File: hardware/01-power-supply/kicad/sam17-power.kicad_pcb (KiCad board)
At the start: 2 copper layers, 100 x 150 mm, 37 parts, among them J1 TerminalBlock_MaiXu_MX126-5.0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, J2 Molex_KK-254_AE-6410-04A_1x04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, J3 TerminalBlock_MaiXu_MX126-5.0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, J4 TerminalBlock_MaiXu_MX126-5.0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, J5 Faston_6.3x0.8mm_PCB_2Leg_P5.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, J6 Molex_KK-254_AE-6410-02A_1x02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, U1 TO-220-3_Vertical, U2 TO-220-3_Vertical, U3 TO-220-3_Vertical

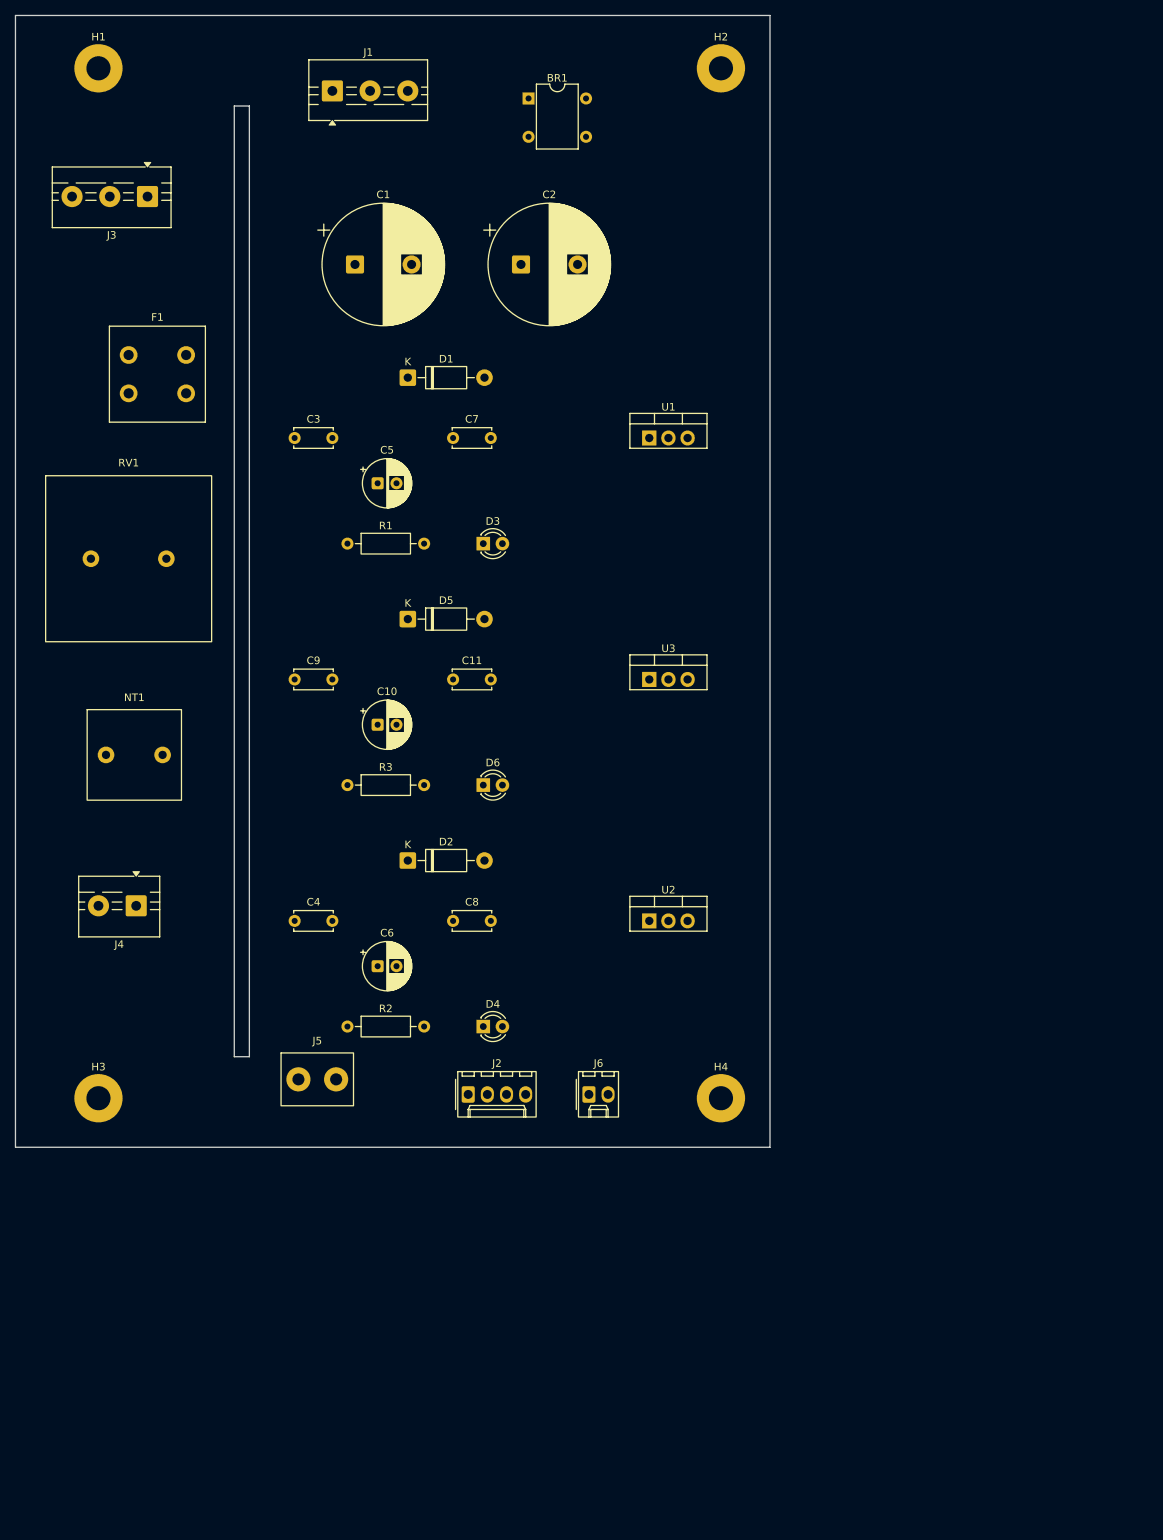
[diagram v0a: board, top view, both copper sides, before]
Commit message: Route module 1 PCB as a verified star ground, no copper pour
Fase 3: la placa queda ruteada entera. DRC de KiCad 0 infracciones y 0 pads
sin conectar. Dos capas, F para carriles y lado de red, B para el arbol de
masa y los bajantes, una sola via en toda la placa.

NO HAY PLANO DE MASA y es a proposito. Un pour une todo con todo por el camino
mas corto, o sea lo contrario de la estrella de sec.7 y del retorno dedicado
de sec.10.1. GND es un arbol que sale de C1.2 (el bulk del riel positivo) y
cada rama muere en su grupo funcional. El retorno del +5V (J6.2) sube por el
canto derecho, la unica columna sin ramas, y entra a la estrella por su propia
via sin tocar ninguna otra.

Que la masa sea un arbol NO SE VE mirando el dibujo — un bucle se ve igual que
una rama — asi que build_pcb.py lo comprueba con union-find sobre los extremos
de los tramos y aborta si encuentra uno. Da 0.

Tampoco se uso autorouter, y no solo por falta del jar: un autorouter respeta
la conectividad y se pasa la topologia por el forro, que aqui es justo lo que
importa.

Lo que fue apareciendo, cada uno con su vuelta:

- Mi verificador comparaba pista contra pista y NO pista contra pad. Con eso
  el trazado salia "limpio" mientras el DRC encontraba cinco cortocircuitos:
  la espina de masa cruzando D5.1 y D2.1, el bajante de -12V rozando el anodo
  de D4, y un LED sin girar. Un pad es cobre igual que una pista; no mirarlo
  era mirar media placa. Ahora se comprueba y da 0.
- Los tres reguladores sacan la salida por el mismo x=89.1, asi que un bajante
  vertical corta a los otros dos. Tres columnas (90/93/97) y el que acaba mas
  a la izquierda gira mas arriba.
- Los tres LED tenian el anodo al lado contrario de su resistencia: la pista
  tenia que atravesar el pad del catodo. Girados 180.
- La espina de masa iba por x=52.5 y D5.1/D2.1 estan en x=52. Movida a x=56,
  por el pasillo de 2.1 mm entre los pads de las resistencias y los ceramicos.
- RED_230V baja de 2.5 a 2.0 mm de separacion. No es relaj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
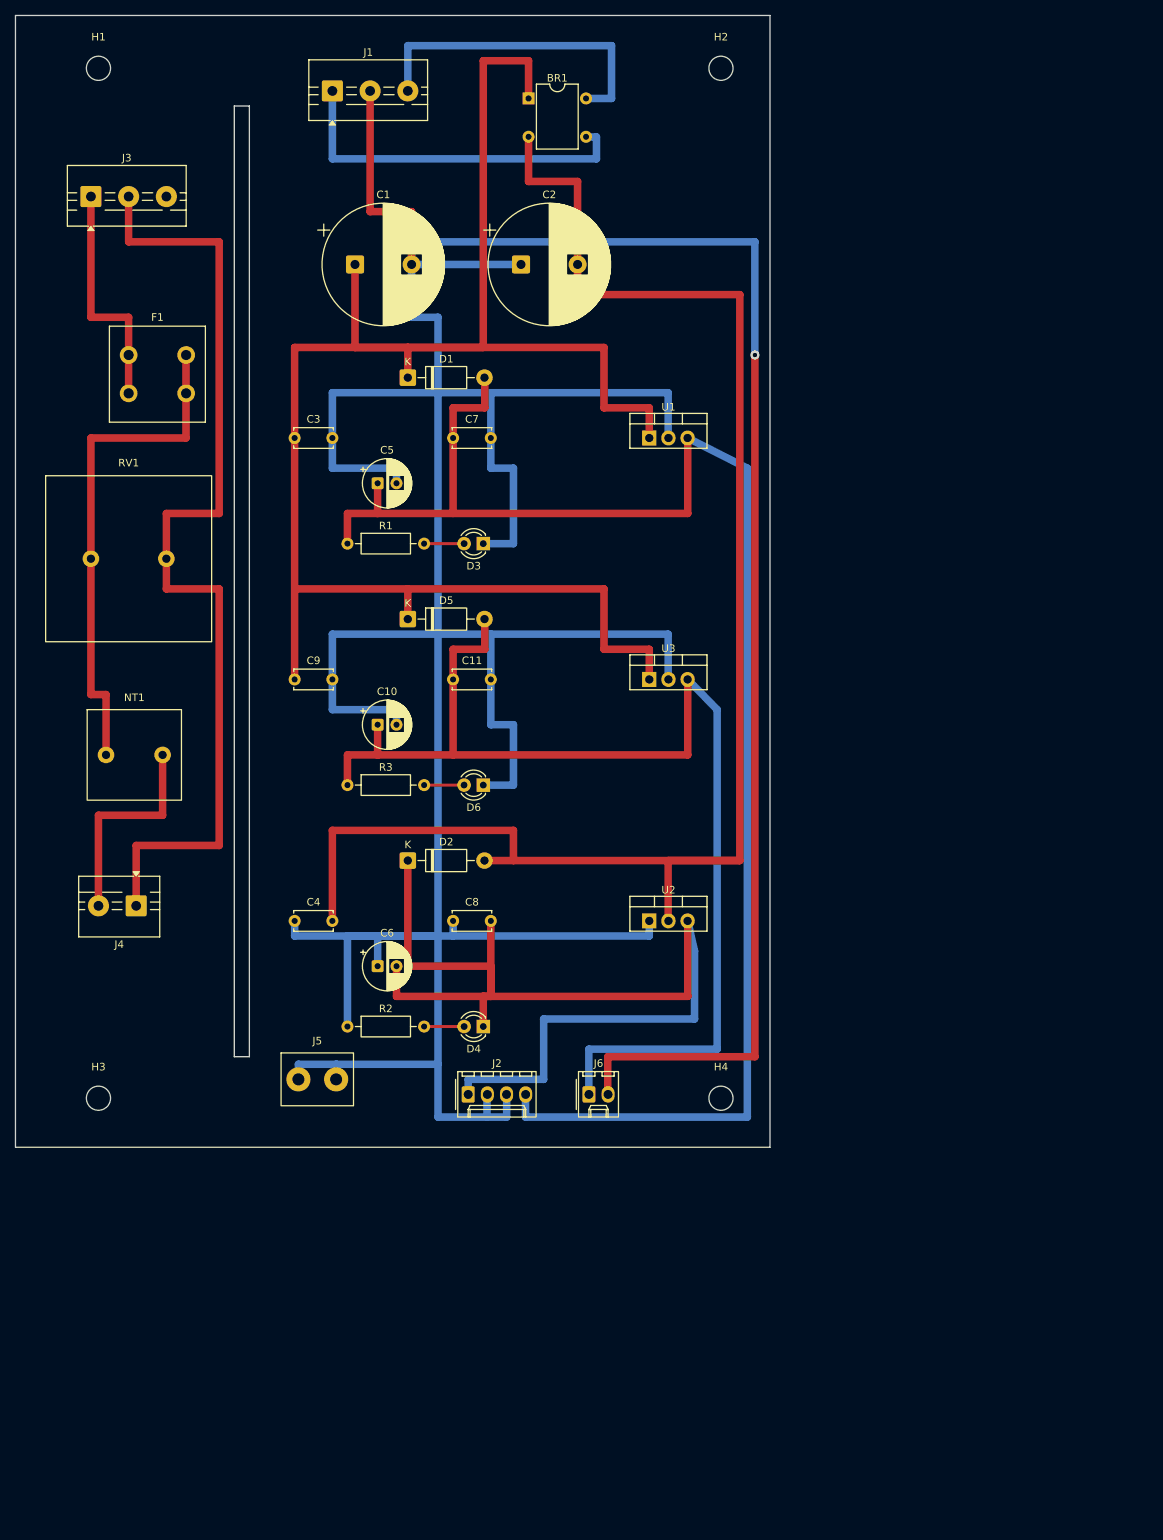
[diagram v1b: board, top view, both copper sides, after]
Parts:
- H1, H2, H3, H4: value MountingHole_3.2mm_M3_Pad -> MountingHole_3.2mm_M3; footprint MountingHole_3.2mm_M3_Pad -> MountingHole_3.2mm_M3
- moved J3 7.50 mm to (10.0, 24.0), turned to 0 degrees
- turned D3 to 180 degrees
- turned D4 to 180 degrees
- turned D6 to 180 degrees
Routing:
- net GND: track 0.00 -> 663.1 mm, vias 0 -> 1
- net /VRAW+: track 0.00 -> 247.0 mm
- net /VRAW-: track 0.00 -> 215.2 mm
- net +12V: track 0.00 -> 212.6 mm
- net +5V: track 0.00 -> 158.9 mm
- net -12V: track 0.00 -> 149.7 mm
- net /N: track 0.00 -> 131.0 mm
- net /L_F: track 0.00 -> 67.6 mm
- net /SEC_A: track 0.00 -> 48.3 mm
- net /SEC_B: track 0.00 -> 43.4 mm
- net /L: track 0.00 -> 31.1 mm
- net /L_TR: track 0.00 -> 28.5 mm
- net Net-(D6-A): track 0.00 -> 5.30 mm
- net Net-(D4-A): track 0.00 -> 5.30 mm
- net Net-(D3-A): track 0.00 -> 5.30 mm

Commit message: Re-lay out module 1 PCB for the LDO respin: 150x200, rail columns
La placa pasa de 100x150 a 150x200. No es capricho: los disipadores pasan de
25x25 a 42x38 (Fischer SK 129/38,1) y tres en fila piden 136 mm de ancho.

DOS DECISIONES DE MAQUETA:

1) La franja de red pasa de columna VERTICAL a la izquierda a fila HORIZONTAL
   arriba, y la barrera con ella. Con la franja vertical harian falta 175 mm de
   ancho (27 de franja + 6 de barrera + 136 de disipadores); en horizontal
   caben en 150.

2) Los tres carriles pasan de filas horizontales a COLUMNAS VERTICALES, cada
   una justo encima de su regulador. En filas, el carril de -12 V tenia que
   cruzar la placa entera para llegar a su regulador, cortando los otros dos.
   En columnas cada riel es autocontenido: bulk arriba, pasivos en su columna,
   regulador debajo, y de ahi al conector.

El crowbar vive en la columna del +12 V, que es el riel que protege.

Comprobaciones, todas en cero: piezas fuera de margen, solapes, piezas sobre la
ranura, pads sin red, cruces de pista y bucles de masa. Barrera red<->SELV
medida en 9.43 mm contra los 6 exigidos.

Los taladros de fijacion siguen sin cobre (sec.13: el puente chasis-masa es
UNO, el de J5) pero cuentan como SELV en la medida de barrera, porque un
separador metalico esta a potencial de chasis.

PENDIENTE: el ruteo. Las pistas se rehacen enteras en la pasada siguiente.

Co-Authored-By: Claude Opus 5 (1M context) <noreply@anthropic.com>
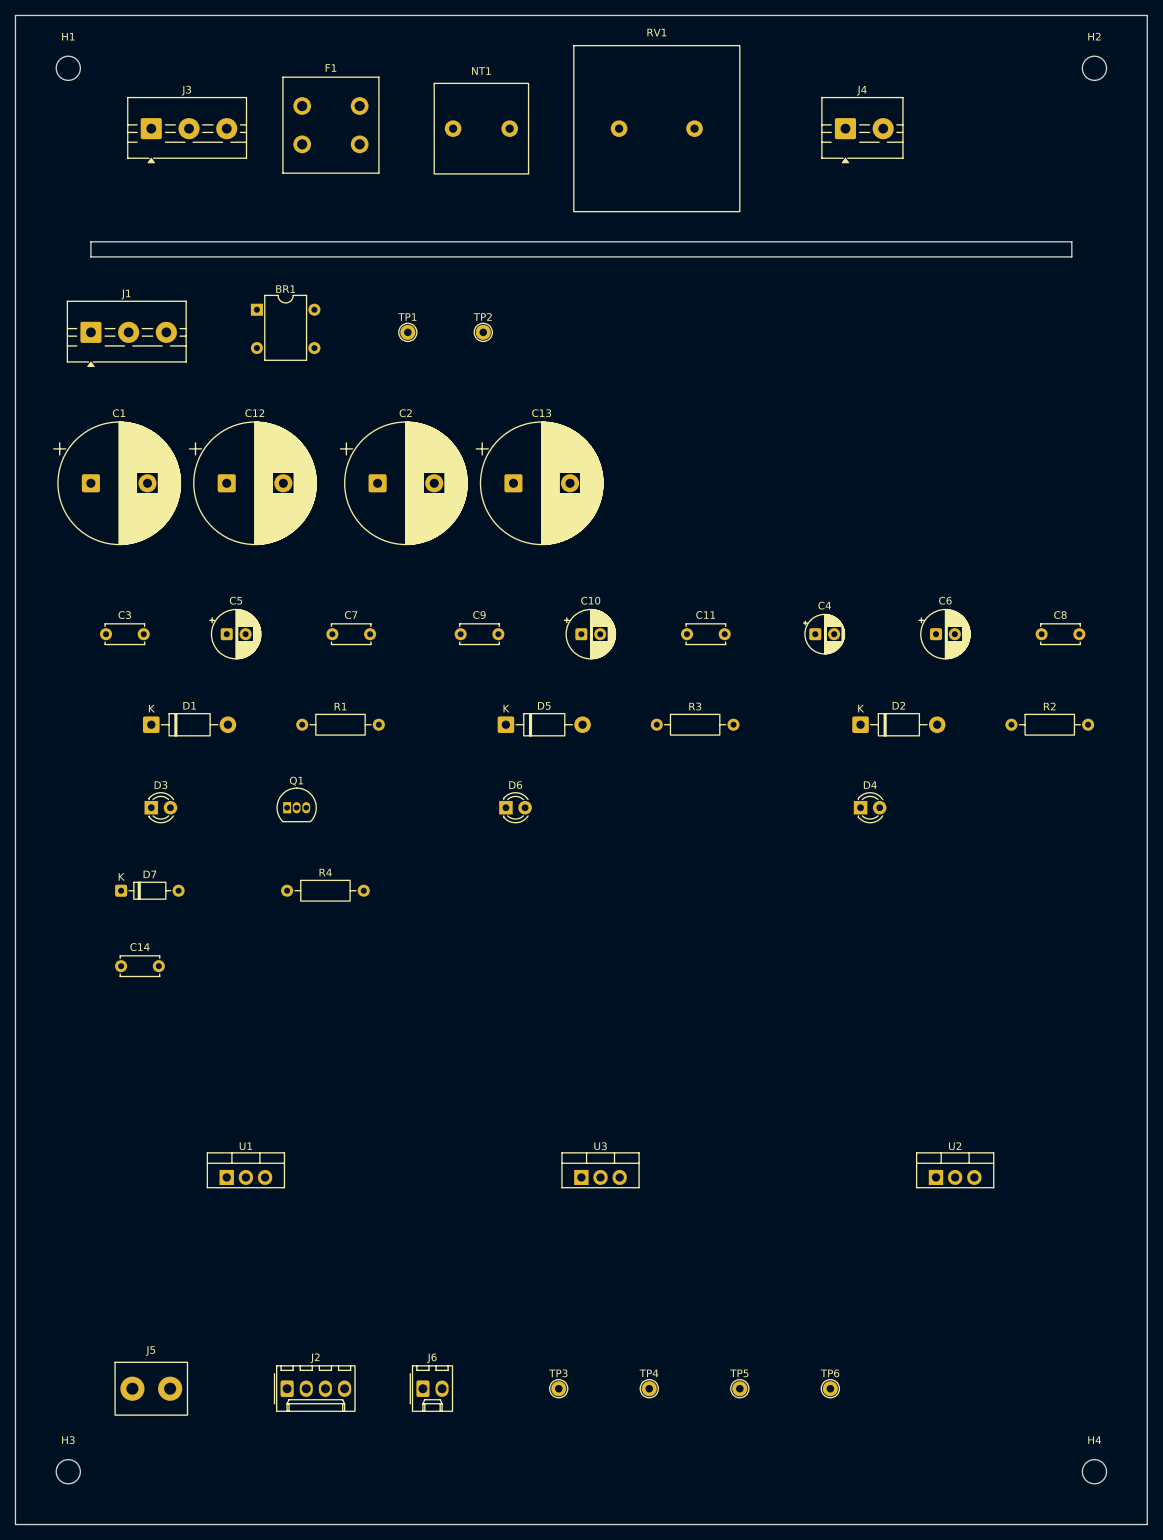
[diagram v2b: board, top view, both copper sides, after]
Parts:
- added C12: CP_Radial_D16.0mm_P7.50mm, CP_Radial_D16.0mm_P7.50mm, F.Cu at (28.0, 62.0)
- added C13: CP_Radial_D16.0mm_P7.50mm, CP_Radial_D16.0mm_P7.50mm, F.Cu at (66.0, 62.0)
- added C14: C_Disc_D5.0mm_W2.5mm_P5.00mm, C_Disc_D5.0mm_W2.5mm_P5.00mm, F.Cu at (14.0, 126.0)
- added D7: D_DO-35_SOD27_P7.62mm_Horizontal, D_DO-35_SOD27_P7.62mm_Horizontal, F.Cu at (14.0, 116.0)
- added Q1: TO-92_Inline, TO-92_Inline, F.Cu at (36.0, 105.0)
- added R4: R_Axial_DIN0207_L6.3mm_D2.5mm_P10.16mm_Horizontal, R_Axial_DIN0207_L6.3mm_D2.5mm_P10.16mm_Horizontal, F.Cu at (36.0, 116.0)
- added TP1: TestPoint_THTPad_D2.0mm_Drill1.0mm, TestPoint_THTPad_D2.0mm_Drill1.0mm, F.Cu at (52.0, 42.0)
- added TP2: TestPoint_THTPad_D2.0mm_Drill1.0mm, TestPoint_THTPad_D2.0mm_Drill1.0mm, F.Cu at (62.0, 42.0)
- added TP3: TestPoint_THTPad_D2.0mm_Drill1.0mm, TestPoint_THTPad_D2.0mm_Drill1.0mm, F.Cu at (72.0, 182.0)
- added TP4: TestPoint_THTPad_D2.0mm_Drill1.0mm, TestPoint_THTPad_D2.0mm_Drill1.0mm, F.Cu at (84.0, 182.0)
- added TP5: TestPoint_THTPad_D2.0mm_Drill1.0mm, TestPoint_THTPad_D2.0mm_Drill1.0mm, F.Cu at (96.0, 182.0)
- added TP6: TestPoint_THTPad_D2.0mm_Drill1.0mm, TestPoint_THTPad_D2.0mm_Drill1.0mm, F.Cu at (108.0, 182.0)
- C4: value C_Disc_D5.0mm_W2.5mm_P5.00mm -> CP_Radial_D5.0mm_P2.50mm; footprint C_Disc_D5.0mm_W2.5mm_P5.00mm -> CP_Radial_D5.0mm_P2.50mm
- moved J4 139.4 mm to (110.0, 15.0), turned to 0 degrees
- moved U1 112.9 mm to (28.0, 154.0)
- moved R2 96.7 mm to (132.0, 94.0)
- moved NT1 94.9 mm to (58.0, 15.0)
- moved RV1 90.3 mm to (80.0, 15.0)
- moved C8 86.8 mm to (136.0, 82.0)
- moved C6 86.1 mm to (122.0, 82.0)
- moved C4 78.8 mm to (106.0, 82.0)
- moved H4 70.0 mm to (143.0, 193.0)
- moved U3 66.6 mm to (75.0, 154.0)
- moved D2 62.6 mm to (112.0, 94.0)
- moved D4 57.8 mm to (112.0, 105.0), turned to 0 degrees
- moved D1 57.2 mm to (18.0, 94.0)
- moved D3 56.2 mm to (18.0, 105.0), turned to 0 degrees
- moved U2 51.0 mm to (122.0, 154.0)
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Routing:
- net GND: track 663.1 -> 0.00 mm, vias 1 -> 0
- net /VRAW+: track 247.0 -> 0.00 mm
- net /VRAW-: track 215.2 -> 0.00 mm
- net +12V: track 212.6 -> 0.00 mm
- net +5V: track 158.9 -> 0.00 mm
- net -12V: track 149.7 -> 0.00 mm
- net /N: track 131.0 -> 0.00 mm
- net /L_F: track 67.6 -> 0.00 mm
- net /SEC_A: track 48.3 -> 0.00 mm
- net /SEC_B: track 43.4 -> 0.00 mm
- net /L: track 31.1 -> 0.00 mm
- net /L_TR: track 28.5 -> 0.00 mm
- net Net-(D6-A): track 5.30 -> 0.00 mm
- net Net-(D4-A): track 5.30 -> 0.00 mm
- net Net-(D3-A): track 5.30 -> 0.00 mm
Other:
- board size 100 x 150 mm -> 150 x 200 mm

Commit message: Route the 650 mA PCB: 226 segments, star ground, DRC clean
DRC de KiCad: 0 infracciones, 0 pads sin conectar, 0 errores de huella. Y los
verificadores propios en cero: cruces, pistas sobre pads ajenos, bucles de
masa, solapes, piezas fuera de margen y piezas sobre la ranura.

226 segmentos, 85 tramos, UNA sola via en toda la placa. La via es la del
retorno dedicado del +5 V, que sube por el canto derecho — la unica columna sin
ramas de masa — y entra a la estrella sin haber tocado ninguna otra rama.

Sigue sin haber plano de masa, y sigue siendo a proposito: un pour une todo con
todo por el camino mas corto, que es lo contrario de la estrella de sec.7. GND
es un arbol de tres ramas (una por columna) mas la de salidas, verificado con
union-find: cero bucles.

Lo que costo varias vueltas, por si sirve de patron:

- Los TP estaban en fila abajo y obligaban a los tres rieles a abanicarse desde
  reguladores separados 47 mm, cruzandose entre ellos. Movidos a la franja
  libre entre el bulk y los pasivos, CADA UNO EN SU COLUMNA: los cruces se
  evaporaron.
- Los LED estaban al principio de su fila y su anodo caia a 28 mm de la
  resistencia. Girados 180 y pegados a ella.
- Los cuatro pads de BR1 estan en dos columnas de dos, asi que de BR1.1 solo se
  puede salir hacia arriba o hacia la izquierda. VRAW+ acabo bajando por el
  canto izquierdo (x=5) y SEC_B mudandose a la cara de soldadura.
- Q1 pasa a TO-92_Inline_Wide: en linea, sus patas a 1.27 mm dejan 0.22 mm
  entre pads, por debajo del margen de la clase. Abiertas a 2.54 el problema
  desaparece y el SCR se dobla igual.

fab/README abre ahora con DOS avisos, no uno: el orden de patillas de BR1 y que
el tab de U2 esta a VRAW-, no a masa. Atornillarlo desnudo al mismo disipador
que U1 es un corto franco al encender.

Ranura verificada en el gerber: el Edge_Cuts tiene vertices en y = 0, 30, 32 y
200, o sea el contorno exterior y el de la fresa.

Co-Authored-By: Claude Opus 5 (1M context) <noreply@anthropic.com>
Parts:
- Q1: value TO-92_Inline -> TO-92_Inline_Wide; footprint TO-92_Inline -> TO-92_Inline_Wide
- moved TP4 113.8 mm to (128.0, 77.0)
- moved TP6 112.4 mm to (68.0, 77.0)
- moved TP3 111.7 mm to (34.0, 77.0)
- moved TP5 105.7 mm to (84.0, 77.0)
- moved TP2 51.7 mm to (100.0, 77.0)
- moved TP1 35.9 mm to (44.0, 77.0)
- moved D3 24.0 mm to (42.0, 105.0), turned to 180 degrees
- moved D4 24.0 mm to (136.0, 105.0), turned to 180 degrees
- moved D6 24.0 mm to (89.0, 105.0), turned to 180 degrees
- moved Q1 4.00 mm to (32.0, 105.0)
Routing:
- net GND: track 0.00 -> 1252.8 mm, vias 0 -> 1
- net /VRAW+: track 0.00 -> 403.0 mm
- net -12V: track 0.00 -> 346.5 mm
- net /VRAW-: track 0.00 -> 256.1 mm
- net +12V: track 0.00 -> 253.9 mm
- net +5V: track 0.00 -> 203.5 mm
- net /N: track 0.00 -> 123.0 mm
- net /L_TR: track 0.00 -> 65.5 mm
- net /L_F: track 0.00 -> 52.4 mm
- net /SEC_A: track 0.00 -> 50.3 mm
- net Net-(D7-A): track 0.00 -> 49.5 mm
- net /L: track 0.00 -> 38.1 mm
- net /SEC_B: track 0.00 -> 28.6 mm
- net Net-(D6-A): track 0.00 -> 19.7 mm
- net Net-(D3-A): track 0.00 -> 19.7 mm
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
